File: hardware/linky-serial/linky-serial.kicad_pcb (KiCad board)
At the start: 2 copper layers, 42.2 x 10.9 mm, 8 parts, among them J1 linky, J2 Conn_01x03_Pin, Q1 BSS123, U1 140814243000

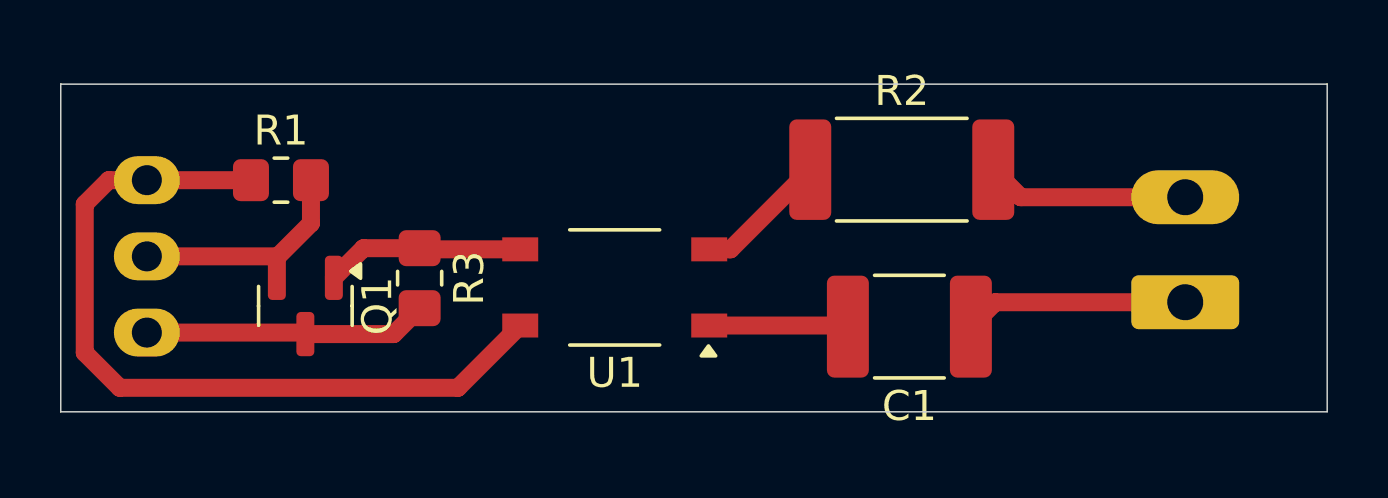
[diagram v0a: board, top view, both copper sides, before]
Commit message: Fix transistor cabling (duh !)
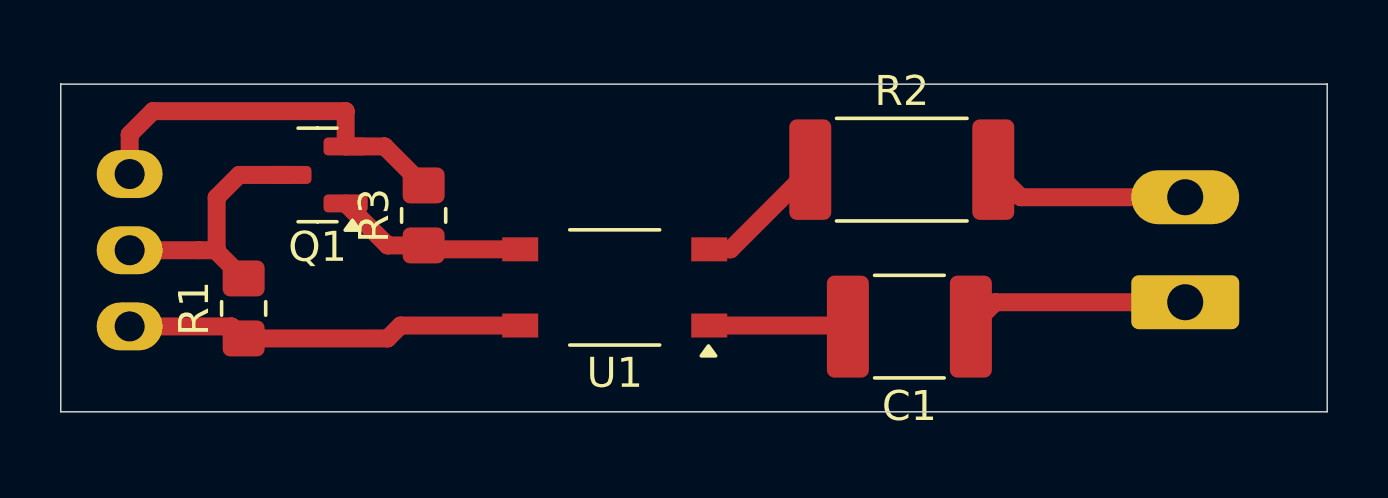
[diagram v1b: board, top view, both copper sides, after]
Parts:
- moved J2 4.91 mm to (143.8, 95.3), turned to 0 degrees
- moved R1 4.45 mm to (147.6, 94.7), turned to 90 degrees
- moved Q1 4.39 mm to (150.1, 90.2), turned to 180 degrees
- moved R3 2.10 mm to (153.6, 91.6), turned to 90 degrees
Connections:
- Q1 pad 2: /TX -> GND
- Q1 pad 3: GND -> /TX
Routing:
- net +5V: track 26.7 -> 13.4 mm
- net GND: track 9.47 -> 13.2 mm
- net /TX: track 7.37 -> 8.70 mm

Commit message: linky interface: update gate resitor value after tests
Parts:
- R3: value 10K -> 4k7
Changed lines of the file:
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@@
 		(tags "resistor handsolder")
 		(property "Reference" "R3"
-			(at 0 -1.65 270)
-			(layer "F.SilkS")
-			(effects
-				(font
-					(size 1 1)
-					(thickness 0.15)
-				)
-			)
-		)
-		(property "Value" "10K"
-			(at 0 1.65 270)
+			(at 0 -1.65 -90)
+			(layer "F.SilkS")
+			(effects
+				(font
+					(size 1 1)
+					(thickness 0.15)
+				)
+			)
+		)
+		(property "Value" "4k7"
+			(at 0 1.65 -90)
 			(layer "F.Fab")
 			(effects
@@
 		)
 		(fp_text user "${REFERENCE}"
-			(at 0 0 270)
+			(at 0 0 -90)
 			(layer "F.Fab")
 			(effects
@@
 		(tags "resistor handsolder")
 		(property "Reference" "R1"
-			(at 0 -1.65 270)
+			(at 0 -1.65 -90)
 			(layer "F.SilkS")
 			(effects
@@
 		)
 		(property "Value" "10K"
-			(at 0 1.65 270)
+			(at 0 1.65 -90)
 			(layer "F.Fab")
 			(effects
@@
 		)
 		(fp_text user "${REFERENCE}"
-			(at 0 0 270)
+			(at 0 0 -90)
 			(layer "F.Fab")
 			(effects
@@
 		(tags "Through hole pin header THT 1x03 2.54mm single row")
 		(property "Reference" "J2"
-			(at 0 2.33 360)
+			(at 0 2.33 0)
 			(layer "B.SilkS")
 			(effects
@@
 		)
 		(property "Value" "Conn_01x03_Pin"
-			(at 0 -7.41 360)
+			(at 0 -7.41 0)
 			(layer "B.Fab")
 			(effects
